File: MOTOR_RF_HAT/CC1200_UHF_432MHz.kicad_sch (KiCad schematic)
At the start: 41 parts, among them J2 SMA, U2 CC1200RHBR, Y2 40MHz

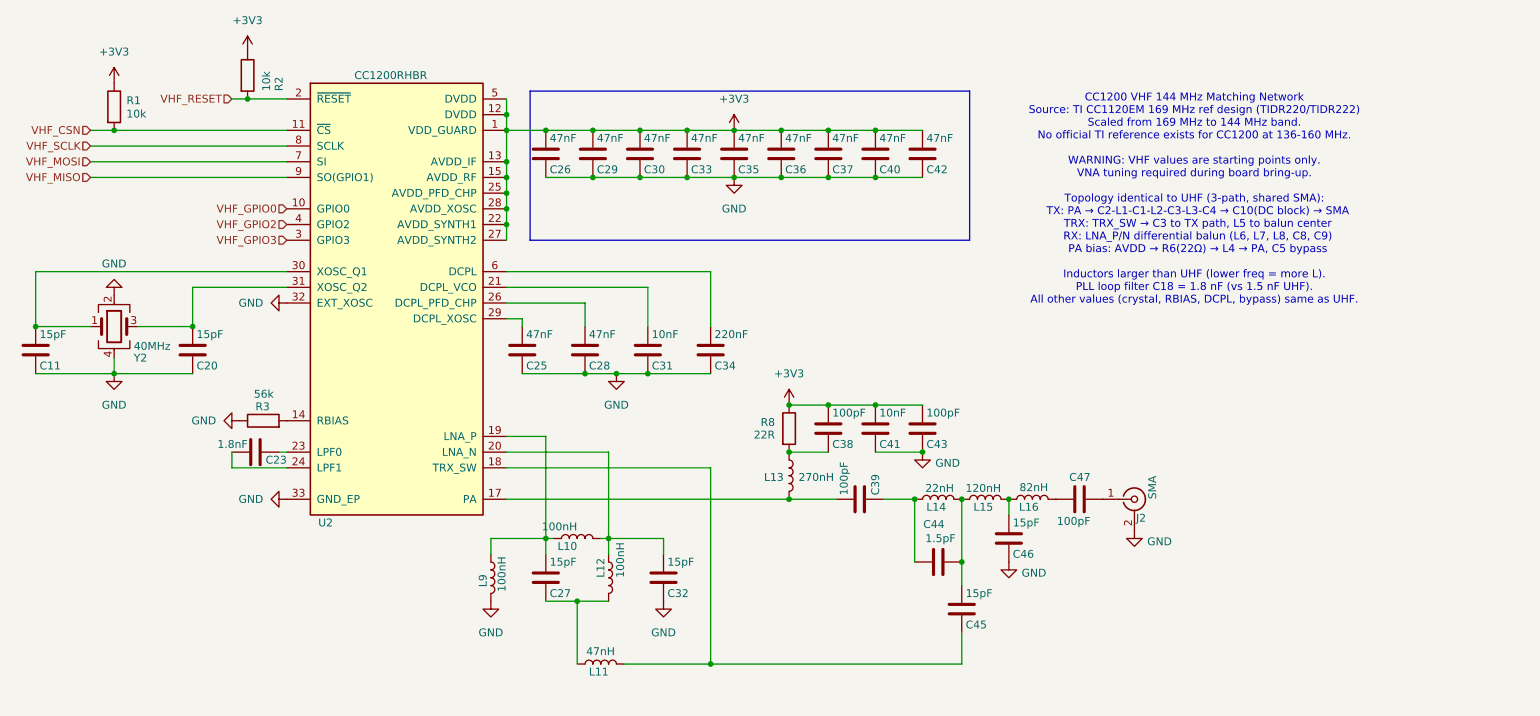
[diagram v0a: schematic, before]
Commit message: MOTOR_RF_HAT: port full RF_HAT project with all libs localized
Copied complete RF_HAT_out KiCad project (schematic + PCB layout +
4 hierarchical sub-sheets) as the base for the combined board.

Changes from original RF_HAT:
- Renamed RF_HAT → MOTOR_RF_HAT in all project/schematic references
- Imported LMR51420YDDCR + XRTC303020D4R7MBCA symbols from personal
  lib into project-local components.kicad_sym
- Copied corresponding footprints + 3D models (SOT-23-6, inductor)
  into components.pretty/ and components.3dshapes/
- Fixed all lib: → components: references in schematics and PCB
- Removed reference/ directory (schematics are now live sub-sheets)
- ERC: 20 violations (19 pre-existing from RF_HAT + 1 from rename)
- Zero external library dependencies — fully self-contained

Ready to add motor driver (A4950E), encoder, and IMU (ADXL345)
sub-sheets. Existing CC1200 UHF/VHF, Pi header, Pico, power,
NeoPixel, and buzzer circuits carry over unchanged.

Co-Authored-By: Claude Opus 4.6 (1M context) <noreply@anthropic.com>
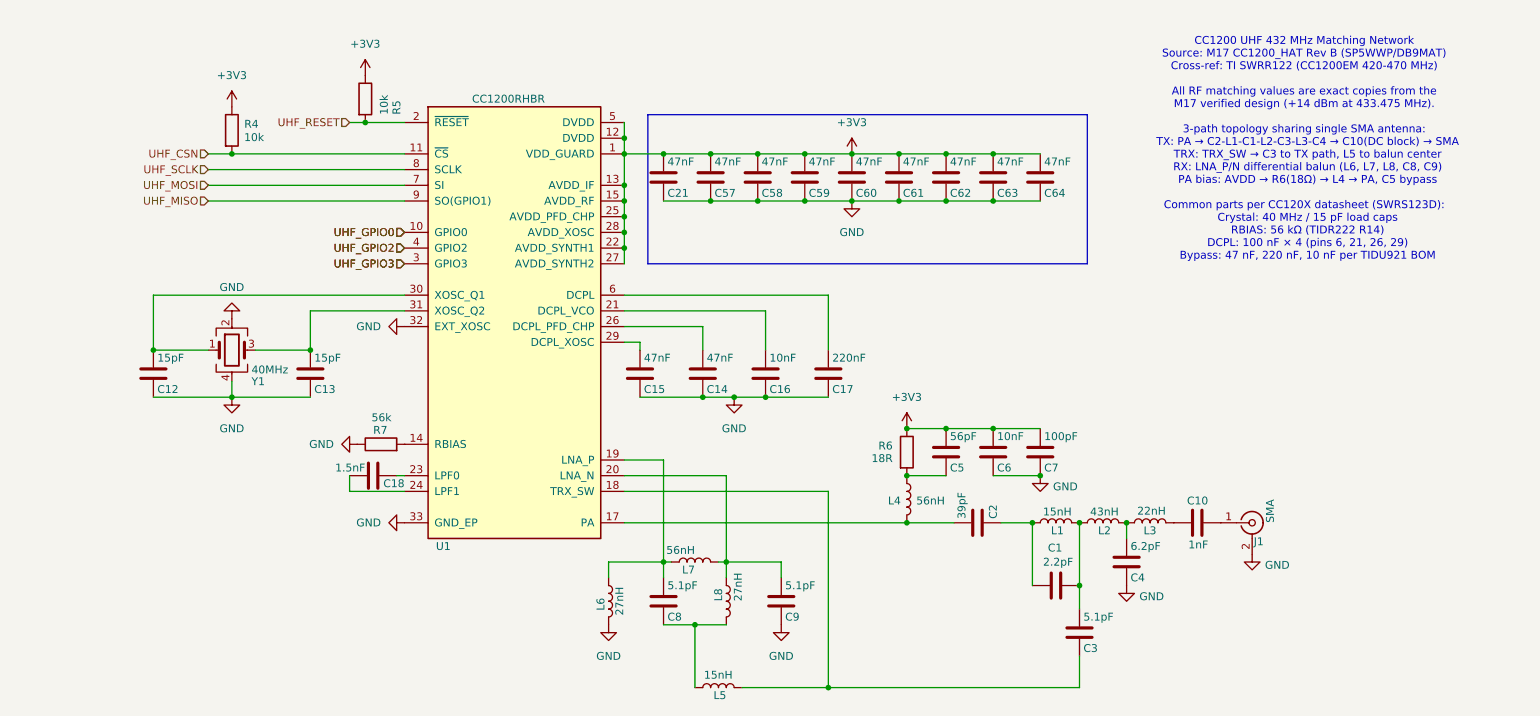
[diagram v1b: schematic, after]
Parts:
- removed C11, C20, C27, C32, C45, C46: 15pF, Capacitor_SMD:C_0603_1608Metric, symbol Device:C
- removed C23: 1.8nF, Capacitor_SMD:C_0603_1608Metric, symbol Device:C
- removed C25, C26, C28, C29, C30, C33, C35, C36, C37, C40, C42: 47nF, Capacitor_SMD:C_0603_1608Metric, symbol Device:C
- removed C31, C41: 10nF, Capacitor_SMD:C_0603_1608Metric, symbol Device:C
- removed C34: 220nF, Capacitor_SMD:C_0603_1608Metric, symbol Device:C
- removed C38, C39, C43, C47: 100pF, Capacitor_SMD:C_0603_1608Metric, symbol Device:C
- removed C44: 1.5pF, Capacitor_SMD:C_0603_1608Metric, symbol Device:C
- removed J2: SMA, Connector_Coaxial:SMA_Amphenol_132289_EdgeMount, symbol Connector:Conn_Coaxial
- removed L10, L12, L9: 100nH, Inductor_SMD:L_0603_1608Metric, symbol Device:L
- removed L11: 47nH, Inductor_SMD:L_0603_1608Metric, symbol Device:L
- removed L13: 270nH, Inductor_SMD:L_0603_1608Metric, symbol Device:L
- removed L14: 22nH, Inductor_SMD:L_0603_1608Metric, symbol Device:L
- removed L15: 120nH, Inductor_SMD:L_0603_1608Metric, symbol Device:L
- removed L16: 82nH, Inductor_SMD:L_0603_1608Metric, symbol Device:L
- removed R1, R2: 10k, Resistor_SMD:R_0603_1608Metric, symbol Device:R
- removed R3: 56k, Resistor_SMD:R_0603_1608Metric, symbol Device:R
- removed R8: 22R, Resistor_SMD:R_0603_1608Metric, symbol Device:R
- removed U2: CC1200RHBR, Package_DFN_QFN:QFN-32-1EP_5x5mm_P0.5mm_EP3.45x3.45mm, symbol RF:CC1200
- removed Y2: 40MHz, Crystal:Crystal_SMD_3225-4Pin_3.2x2.5mm, symbol Device:Crystal_GND24
- added C1: 2.2pF, Capacitor_SMD:C_0603_1608Metric, symbol Device:C
- added C10: 1nF, Capacitor_SMD:C_0603_1608Metric, symbol Device:C
- added C12, C13: 15pF, Capacitor_SMD:C_0603_1608Metric, symbol Device:C
- added C14, C15, C21, C57, C58, C59, C60, C61, C62, C63, C64: 47nF, Capacitor_SMD:C_0603_1608Metric, symbol Device:C
- added C16, C6: 10nF, Capacitor_SMD:C_0603_1608Metric, symbol Device:C
- added C17: 220nF, Capacitor_SMD:C_0603_1608Metric, symbol Device:C
- added C18: 1.5nF, Capacitor_SMD:C_0603_1608Metric, symbol Device:C
- added C2: 39pF, Capacitor_SMD:C_0603_1608Metric, symbol Device:C
- added C3, C8, C9: 5.1pF, Capacitor_SMD:C_0603_1608Metric, symbol Device:C
- added C4: 6.2pF, Capacitor_SMD:C_0603_1608Metric, symbol Device:C
- added C5: 56pF, Capacitor_SMD:C_0603_1608Metric, symbol Device:C
- added C7: 100pF, Capacitor_SMD:C_0603_1608Metric, symbol Device:C
- added J1: SMA, Connector_Coaxial:SMA_Amphenol_132289_EdgeMount, symbol Connector:Conn_Coaxial
- added L1, L5: 15nH, Inductor_SMD:L_0603_1608Metric, symbol Device:L
- added L2: 43nH, Inductor_SMD:L_0603_1608Metric, symbol Device:L
- added L3: 22nH, Inductor_SMD:L_0603_1608Metric, symbol Device:L
- added L4, L7: 56nH, Inductor_SMD:L_0603_1608Metric, symbol Device:L
- added L6, L8: 27nH, Inductor_SMD:L_0603_1608Metric, symbol Device:L
- added R4, R5: 10k, Resistor_SMD:R_0603_1608Metric, symbol Device:R
- added R6: 18R, Resistor_SMD:R_0603_1608Metric, symbol Device:R
- added R7: 56k, Resistor_SMD:R_0603_1608Metric, symbol Device:R
- added U1: CC1200RHBR, Package_DFN_QFN:QFN-32-1EP_5x5mm_P0.5mm_EP3.45x3.45mm, symbol RF:CC1200
- added Y1: 40MHz, Crystal:Crystal_SMD_3225-4Pin_3.2x2.5mm, symbol Device:Crystal_GND24
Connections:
- net +3V3: now also C21.1, C5.1, C57.1, C58.1, C59.1, C6.1, C60.1, C61.1, C62.1, C63.1, C64.1, C7.1, R4.1, R5.1, R6.1, U1.1 (VDD_GUARD), U1.12 (DVDD), U1.13 (AVDD_IF), U1.15 (AVDD_RF), U1.22 (AVDD_SYNTH1), U1.25 (AVDD_PFD_CHP), U1.27 (AVDD_SYNTH2), U1.28 (AVDD_XOSC), U1.5 (DVDD)
- net GND: now also C12.2, C13.2, C14.2, C15.2, C16.2, C17.2, C21.2, C4.2, C57.2, C58.2, C59.2, C6.2, C60.2, C61.2, C62.2, C63.2, C64.2, C7.2, C9.2, J1.2 (Ext), L6.2, R7.1, U1.32 (EXT_XOSC), U1.33 (GND_EP), Y1.2, Y1.4
- new net: C16.1, U1.21 (DCPL_VCO)
- new net: C1.2, C3.1, L1.2, L2.1
- new net: C4.1, L2.2, L3.1
- new net: C18.1, U1.24 (LPF1)
- new net: C18.2, U1.23 (LPF0)
- new net: C2.1, L4.2, U1.17 (PA)
- new net: C1.1, C2.2, L1.1
- new net: C12.1, U1.30 (XOSC_Q1), Y1.1
- new net: R7.2, U1.14 (RBIAS)
- new net: C3.2, L5.2, U1.18 (TRX_SW)
- new net: C8.1, L6.1, L7.1, U1.19 (LNA_P)
- new net: C9.1, L7.2, L8.1, U1.20 (LNA_N)
- new net: C14.1, U1.26 (DCPL_PFD_CHP)
- new net: C15.1, U1.29 (DCPL_XOSC)
- new net: C13.1, U1.31 (XOSC_Q2), Y1.3
- new net: C17.1, U1.6 (DCPL)
- new net: C10.1, L3.2
- new net: C10.2, J1.1 (In)
- new net: C8.2, L5.1, L8.2
- new net: C5.2, L4.1, R6.2
- new net UHF_CSN: R4.2, U1.11 (~{CS})
- new net UHF_GPIO0: U1.10 (GPIO0)
- new net UHF_GPIO2: U1.4 (GPIO2)
- new net UHF_GPIO3: U1.3 (GPIO3)
- new net UHF_MISO: U1.9 (SO(GPIO1))
- new net UHF_MOSI: U1.7 (SI)
- new net UHF_RESET: R5.2, U1.2 (~{RESET})
- new net UHF_SCLK: U1.8 (SCLK)
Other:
- note added: "CC1200 UHF 432 MHz Matching Network Source: M17 CC1200_HAT Rev B (SP5WWP/DB9MAT) Cross-ref: TI SWRR122 (CC1200EM 420-470 MHz) All RF matching values are exact copies from the M17 verified design (+14 dBm at 433.475 MHz). 3-path topology sharing single SMA antenna: TX: PA → C2-L1-C1-L2-C3-L3-C4 → C10(DC block) → SMA TRX: TRX_SW → C3 to TX path, L5 to balun center RX: LNA_P/N differential balun (L6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"
- note removed: "CC1200 VHF 144 MHz Matching Network Source: TI CC1120EM 169 MHz ref design (TIDR220/TIDR222) Scaled from 169 MHz to 144 MHz band. No official TI reference exists for CC1200 at 136-160 MHz. WARNING: VHF values are starting points only. VNA tuning required during board bring-up. Topology identical to UHF (3-path, shared SMA): TX: PA → C2-L1-C1-L2-C3-L3-C4 → C10(DC block) → SMA TRX: TRX_SW → C3 to T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"
- title: RF_HAT -> MOTOR_RF_HAT

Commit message: MOTOR_RF_HAT: add TestPoint lib alias to fix persistent smallpad errors
KiCad's lib_symbols cache keeps reverting footprint refs to
TestPoint:smallpad on save. Added TestPoint as a footprint library
alias pointing to components.pretty so both TestPoint:smallpad and
components:smallpad resolve to the same local footprint.

Co-Authored-By: Claude Opus 4.6 (1M context) <noreply@anthropic.com>
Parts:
- renumbered C13 to C12, C18 to C13, C15 to C20, C21 to C22, C8 to C24, C14 to C26, C57 to C27, C58 to C30, C16 to C31, C9 to C33, C59 to C34, C17 to C36, C60 to C38, C61 to C42, C62 to C46, C5 to C47, C2 to C49, C63 to C50, C6 to C51, C64 to C53, C7 to C54, C1 to C55, C3 to C57, C4 to C58, C10 to C59, C12 to C9, J1 to J5, L4 to L11, L1 to L15, L2 to L16, L3 to L17, L5 to L8, L8 to L9, R6 to R10, R5 to R7, R7 to R8, U1 to U5, Y1 to Y2

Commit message: MOTOR_RF_HAT: 0805→0603 passives, encoder caps 100nF→100pF
- Changed all capacitor and resistor footprints from 0805 to 0603
  across all schematic sheets (CC1200 UHF/VHF, root, azimuth,
  elevation, encoders)
- Fixed encoder RC filter caps C68-C71 from 100nF to 100pF
  (fc = 15.9 MHz, transparent to 35 kHz encoder signal)

Co-Authored-By: Claude Opus 4.6 (1M context) <noreply@anthropic.com>
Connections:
- net UHF_GPIO2: no longer names the net of U5.4 (GPIO2)
- net UHF_GPIO3: no longer names the net of U5.3 (GPIO3)
- no-connect marks 0 -> 2
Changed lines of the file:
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@@
 		(color 0 0 0 0)
 	)
+	(no_connect
+		(at 99.06 74.93)
+	)
+	(no_connect
+		(at 99.06 72.39)
+	)
 	(wire
 		(pts
@@
 			(width 0)
 			(type default)
-		)
-	)
-	(hierarchical_label "UHF_GPIO2"
-		(shape input)
-		(at 99.06 72.39 180)
-		(effects
-			(font
-				(size 1.27 1.27)
-			)
-			(justify right)
-		)
-	)
-	(hierarchical_label "UHF_GPIO3"
-		(shape input)
-		(at 99.06 74.93 180)
-		(effects
-			(font
-				(size 1.27 1.27)
-			)
-			(justify right)
 		)
 	)
@@
 		)
 	)
-	(hierarchical_label "UHF_GPIO3"
-		(shape input)
-		(at 99.06 74.93 180)
-		(effects
-			(font
-				(size 1.27 1.27)
-			)
-			(justify right)
-		)
-	)
 	(hierarchical_label "UHF_RESET"
 		(shape input)
@@
 		(effects
 			(font
-				(size 1.27 1.27)
-			)
-			(justify right)
-		)
-	)
-	(hierarchical_label "UHF_GPIO2"
-		(shape input)
-		(at 99.06 72.39 180)
-		(effects
-			(font
